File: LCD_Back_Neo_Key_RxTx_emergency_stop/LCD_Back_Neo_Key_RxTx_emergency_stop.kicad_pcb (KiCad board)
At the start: 2 copper layers, 105.5 x 101.5 mm, 23 parts, among them J1 Screw_Terminal_01x14, J2 Conn_01x20_Female, J3 Conn_01x08_Male_KeyPad, J4 Display_support_pin, J5 Display_support_pin, K1 FINDER-34.51, K2 FINDER-34.51, K3 FINDER-34.51, K4 FINDER-34.51, Q1 BC337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

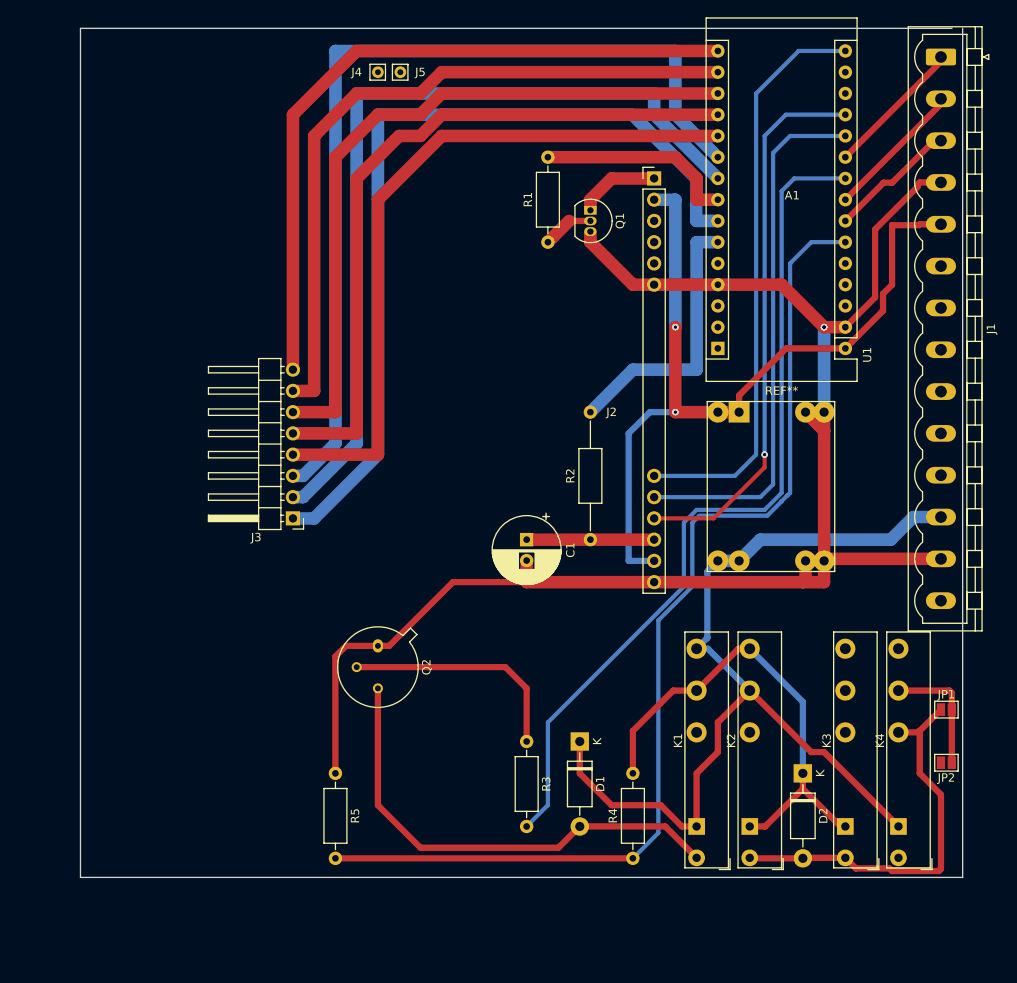
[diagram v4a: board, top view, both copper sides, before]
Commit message: contact all on PCB
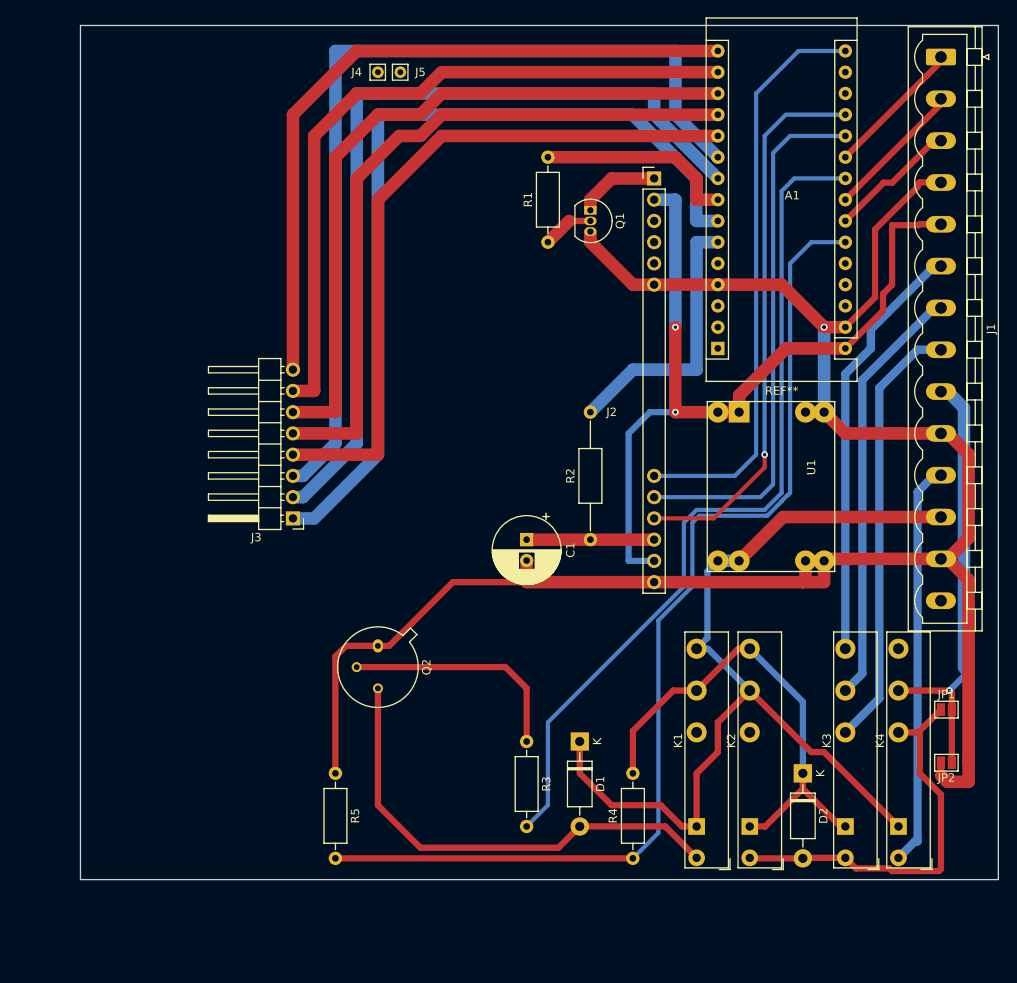
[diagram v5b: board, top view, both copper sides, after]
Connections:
- J1 pad 6: ScrewTerm8-EmrgencyRelay12 -> ScrewTerm9-EmrgencyRelay14
- J1 pad 7: ScrewTerm9-EmrgencyRelay14 -> ScrewTerm10-EmrgencyRelay11
- J1 pad 8: ScrewTerm10-EmrgencyRelay11 -> ScrewTerm8-EmrgencyRelay12
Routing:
- net ScrewTerm8-EmrgencyRelay12: track 0.00 -> 52.1 mm
- net ScrewTerm9-EmrgencyRelay14: track 0.00 -> 50.9 mm
- net ScrewTerm10-EmrgencyRelay11: track 0.00 -> 50.9 mm
- net ScrewTerm13-EmergencyStopSwitch3: track 0.00 -> 48.5 mm
- net GND: track 190.8 -> 238.3 mm
- net ScrewTerm11-EmergencyStopSwitch1: track 14.8 -> 52.9 mm, vias 0 -> 1
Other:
- board size 105.5 x 101.5 mm -> 109.7 x 102.1 mm
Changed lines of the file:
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@@
     (thickness 1.6)
     (drawings 4)
-    (tracks 238)
+    (tracks 271)
     (zones 0)
     (modules 23)
@@
   )
   (setup
-    (last_trace_width 0.75)
+    (last_trace_width 1)
     (user_trace_width 0.5)
     (user_trace_width 0.75)
+    (user_trace_width 1)
     (user_trace_width 1.5)
     (trace_clearance 0.2)
@@
     (descr "Longri ")
     (tags "Longri DCDC-Converter")
-    (fp_text reference U1 (at -4.31 -5.17 90) (layer F.SilkS)
+    (fp_text reference U1 (at 9.144 1.524 90) (layer F.SilkS)
       (effects (font (size 1 1) (thickness 0.15)))
     )
@@
       (net 10 VCC-5V))
     (pad 6 thru_hole oval (at 25 0 270) (size 2 3.6) (drill 1.4) (layers *.Cu *.Mask)
+      (net 46 ScrewTerm9-EmrgencyRelay14))
+    (pad 7 thru_hole oval (at 30 0 270) (size 2 3.6) (drill 1.4) (layers *.Cu *.Mask)
+      (net 47 ScrewTerm10-EmrgencyRelay11))
+    (pad 8 thru_hole oval (at 35 0 270) (size 2 3.6) (drill 1.4) (layers *.Cu *.Mask)
       (net 45 ScrewTerm8-EmrgencyRelay12))
-    (pad 7 thru_hole oval (at 30 0 270) (size 2 3.6) (drill 1.4) (layers *.Cu *.Mask)
-      (net 46 ScrewTerm9-EmrgencyRelay14))
-    (pad 8 thru_hole oval (at 35 0 270) (size 2 3.6) (drill 1.4) (layers *.Cu *.Mask)
-      (net 47 ScrewTerm10-EmrgencyRelay11))
     (pad 9 thru_hole oval (at 40 0 270) (size 2 3.6) (drill 1.4) (layers *.Cu *.Mask)
       (net 48 ScrewTerm11-EmergencyStopSwitch1))
@@
     )
   )
-  (gr_line (start 104.14 32.86) (end 104.14 134.36) (layer Edge.Cuts) (width 0.05))
-  (gr_line (start 208.34 32.86) (end 104.14 32.86) (layer Edge.Cuts) (width 0.05))
-  (gr_line (start 209.61 32.86) (end 209.61 134.36) (layer Edge.Cuts) (width 0.05))
-  (gr_line (start 104.14 134.36) (end 209.61 134.36) (layer Edge.Cuts) (width 0.05))
+  (gr_line (start 104.14 32.512) (end 104.14 134.62) (layer Edge.Cuts) (width 0.05))
+  (gr_line (start 213.868 32.512) (end 104.14 32.512) (layer Edge.Cuts) (width 0.05))
+  (gr_line (start 213.868 32.512) (end 213.868 134.62) (layer Edge.Cuts) (width 0.05))
+  (gr_line (start 104.14 134.62) (end 213.868 134.62) (layer Edge.Cuts) (width 0.05))
   (segment (start 185.42 63.5) (end 185.42 63.5) (width 0.25) (layer F.Cu) (net 9))
   (segment (start 157.48 96.48) (end 157.48 99.06) (width 1.5) (layer F.Cu) (net 9))
@@
   (segment (start 193.04 99.06) (end 193.04 96.52) (width 1.5) (layer F.Cu) (net 9))
   (segment (start 193.04 96.52) (end 190.82 96.52) (width 1.5) (layer F.Cu) (net 9))
-  (segment (start 193.04 80.96) (end 193.04 78.74) (width 1.5) (layer F.Cu) (net 9))
-  (segment (start 193.04 80.96) (end 190.82 78.74) (width 1.5) (layer F.Cu) (net 9))
-  (segment (start 193.04 93.98) (end 193.04 94.3) (width 1.5) (layer F.Cu) (net 9))
-  (segment (start 193.04 96.52) (end 193.04 93.98) (width 1.5) (layer F.Cu) (net 9))
-  (segment (start 193.04 93.98) (end 193.04 80.96) (width 1.5) (layer F.Cu) (net 9))
   (segment (start 190.82 96.52) (end 190.82 98.74) (width 1.5) (layer F.Cu) (net 9))
   (segment (start 190.82 98.74) (end 190.5 99.06) (width 1.5) (layer F.Cu) (net 9))
@@
   (segment (start 199.136 65.024) (end 199.136 56.896) (width 0.75) (layer F.Cu) (net 9))
   (segment (start 195.58 68.58) (end 199.136 65.024) (width 0.75) (layer F.Cu) (net 9))
+  (segment (start 207.81 81.28) (end 207.01 81.28) (width 1.5) (layer F.Cu) (net 9))
+  (segment (start 210.31 83.78) (end 207.81 81.28) (width 1.5) (layer F.Cu) (net 9))
+  (segment (start 210.31 93.78) (end 210.31 83.78) (width 1.5) (layer F.Cu) (net 9))
+  (segment (start 207.81 96.28) (end 210.31 93.78) (width 1.5) (layer F.Cu) (net 9))
+  (segment (start 207.01 96.28) (end 207.81 96.28) (width 1.5) (layer F.Cu) (net 9))
+  (segment (start 207.81 96.28) (end 210.312 98.782) (width 1.5) (layer F.Cu) (net 9))
+  (segment (start 210.312 98.782) (end 210.312 120.396) (width 1.5) (layer F.Cu) (net 9))
+  (segment (start 210.312 120.396) (end 210.312 122.936) (width 1.5) (layer F.Cu) (net 9))
+  (segment (start 210.312 122.936) (end 210.312 122.936) (width 1.5) (layer F.Cu) (net 9))
+  (segment (start 210.312 122.936) (end 207.772 122.936) (width 1.5) (layer F.Cu) (net 9))
+  (segment (start 207.01 122.174) (end 207.01 120.65) (width 0.75) (layer F.Cu) (net 9))
+  (segment (start 207.772 122.936) (end 207.01 122.174) (width 1.5) (layer F.Cu) (net 9))
+  (segment (start 195.58 81.28) (end 193.04 78.74) (width 1.5) (layer F.Cu) (net 9))
+  (segment (start 207.01 81.28) (end 195.58 81.28) (width 1.5) (layer F.Cu) (net 9))
+  (segment (start 190.82 78.74) (end 193.04 78.74) (width 1.5) (layer F.Cu) (net 9))
   (segment (start 180.34 78.74) (end 182.88 78.74) (width 1.5) (layer F.Cu) (net 10))
   (segment (start 180.34 78.74) (end 175.26 78.74) (width 1.5) (layer F.Cu) (net 10))
@@
   (segment (start 201.168 63.5) (end 200.08601 64.58199) (width 0.75) (layer F.Cu) (net 10))
   (segment (start 201.168 56.388) (end 201.168 63.5) (width 0.75) (layer F.Cu) (net 10))
-  (segment (start 182.88 76.74) (end 188.5 71.12) (width 0.75) (layer F.Cu) (net 10))
-  (segment (start 182.88 78.74) (end 182.88 76.74) (width 0.75) (layer F.Cu) (net 10))
-  (segment (start 188.5 71.12) (end 195.58 71.12) (width 0.75) (layer F.Cu) (net 10))
+  (segment (start 182.88 76.74) (end 188.5 71.12) (width 1.5) (layer F.Cu) (net 10))
+  (segment (start 182.88 78.74) (end 182.88 76.74) (width 1.5) (layer F.Cu) (net 10))
+  (segment (start 188.5 71.12) (end 195.58 71.12) (width 1.5) (layer F.Cu) (net 10))
   (segment (start 180.34 58.42) (end 177.8 58.42) (width 1.5) (layer B.Cu) (net 11))
   (segment (start 177.8 58.42) (end 177.8 73.66) (width 1.5) (layer B.Cu) (net 11))
@@
   (segment (start 193.04 119.38) (end 200.66 127) (width 0.75) (layer F.Cu) (net 34))
   (segment (start 200.66 127) (end 201.93 128.27) (width 0.75) (layer F.Cu) (net 34))
-  (segment (start 203.71 91.28) (end 201.01 93.98) (width 1.5) (layer B.Cu) (net 34))
-  (segment (start 207.01 91.28) (end 203.71 91.28) (width 1.5) (layer B.Cu) (net 34))
-  (segment (start 185.42 93.98) (end 182.88 96.52) (width 1.5) (layer B.Cu) (net 34))
-  (segment (start 201.01 93.98) (end 185.42 93.98) (width 1.5) (layer B.Cu) (net 34))
   (segment (start 178.999999 105.820001) (end 177.8 107.02) (width 0.75) (layer B.Cu) (net 34))
   (segment (start 179.090001 105.729999) (end 178.999999 105.820001) (width 0.75) (layer B.Cu) (net 34))
   (segment (start 179.090001 97.769999) (end 179.090001 105.729999) (width 0.75) (layer B.Cu) (net 34))
   (segment (start 180.34 96.52) (end 179.090001 97.769999) (width 0.75) (layer B.Cu) (net 34))
+  (segment (start 188.12 91.28) (end 182.88 96.52) (width 1.5) (layer F.Cu) (net 34))
+  (segment (start 207.01 91.28) (end 188.12 91.28) (width 1.5) (layer F.Cu) (net 34))
   (segment (start 157.48 111.76) (end 157.48 118.11) (width 0.75) (layer F.Cu) (net 37))
   (segment (start 137.16 109.22) (end 154.94 109.22) (width 0.75) (layer F.Cu) (net 37))
@@
   (segment (start 207.01 133.35) (end 207.01 124.46) (width 0.75) (layer F.Cu) (net 44))
   (segment (start 204.47 116.84) (end 207.01 114.3) (width 0.75) (layer F.Cu) (net 44))
+  (segment (start 199.644 112.956) (end 195.58 117.02) (width 1) (layer B.Cu) (net 45))
+  (segment (start 199.644 75.846) (end 199.644 112.956) (width 1) (layer B.Cu) (net 45))
+  (segment (start 207.01 71.28) (end 204.21 71.28) (width 1) (layer B.Cu) (net 45))
+  (segment (start 204.21 71.28) (end 199.644 75.846) (width 1) (layer B.Cu) (net 45))
+  (segment (start 206.21 61.28) (end 198.628 68.862) (width 1) (layer B.Cu) (net 46))
+  (segment (start 207.01 61.28) (end 206.21 61.28) (width 1) (layer B.Cu) (net 46))
+  (segment (start 198.628 68.862) (end 198.628 71.12) (width 1) (layer B.Cu) (net 46))
+  (segment (start 198.628 71.12) (end 195.58 74.168) (width 1) (layer B.Cu) (net 46))
+  (segment (start 195.58 74.168) (end 195.58 107.02) (width 1) (layer B.Cu) (net 46))
+  (segment (start 197.612 109.988) (end 195.58 112.02) (width 1) (layer B.Cu) (net 47))
+  (segment (start 197.612 74.878) (end 197.612 109.988) (width 1) (layer B.Cu) (net 47))
+  (segment (start 207.01 66.28) (end 206.21 66.28) (width 1) (layer B.Cu) (net 47))
+  (segment (start 206.21 66.28) (end 197.612 74.878) (width 1) (layer B.Cu) (net 47))
   (segment (start 201.93 112.02) (end 208.02 112.02) (width 0.75) (layer F.Cu) (net 48))
   (segment (start 208.31 112.31) (end 208.31 114.3) (width 0.75) (layer F.Cu) (net 48))
   (segment (start 208.02 112.02) (end 208.31 112.31) (width 0.75) (layer F.Cu) (net 48))
   (segment (start 208.31 114.3) (end 208.31 120.65) (width 0.75) (layer F.Cu) (net 48))
+  (segment (start 209.76001 78.23001) (end 209.76001 109.26399) (width 1.5) (layer B.Cu) (net 48))
+  (segment (start 207.01 76.28) (end 207.81 76.28) (width 1.5) (layer B.Cu) (net 48))
+  (segment (start 207.81 76.28) (end 209.76001 78.23001) (width 1.5) (layer B.Cu) (net 48))
+  (segment (start 208.02 112.02) (end 208.02 112.02) (width 0.75) (layer F.Cu) (net 48))
+  (via (at 208.02 112.02) (size 0.8) (drill 0.4) (layers F.Cu B.Cu) (net 48))
+  (segment (start 209.76001 110.27999) (end 208.02 112.02) (width 0.75) (layer B.Cu) (net 48))
+  (segment (start 209.76001 109.26399) (end 209.76001 110.27999) (width 0.75) (layer B.Cu) (net 48))
+  (segment (start 206.21 86.28) (end 204.216 88.274) (width 1) (layer B.Cu) (net 49))
+  (segment (start 207.01 86.28) (end 206.21 86.28) (width 1) (layer B.Cu) (net 49))
+  (segment (start 204.216 88.274) (end 204.216 130.048) (width 1) (layer B.Cu) (net 49))
+  (segment (start 203.902 130.048) (end 201.93 132.02) (width 1) (layer B.Cu) (net 49))
+  (segment (start 204.216 130.048) (end 203.902 130.048) (width 1) (layer B.Cu) (net 49))
 )

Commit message: move keyboard connector
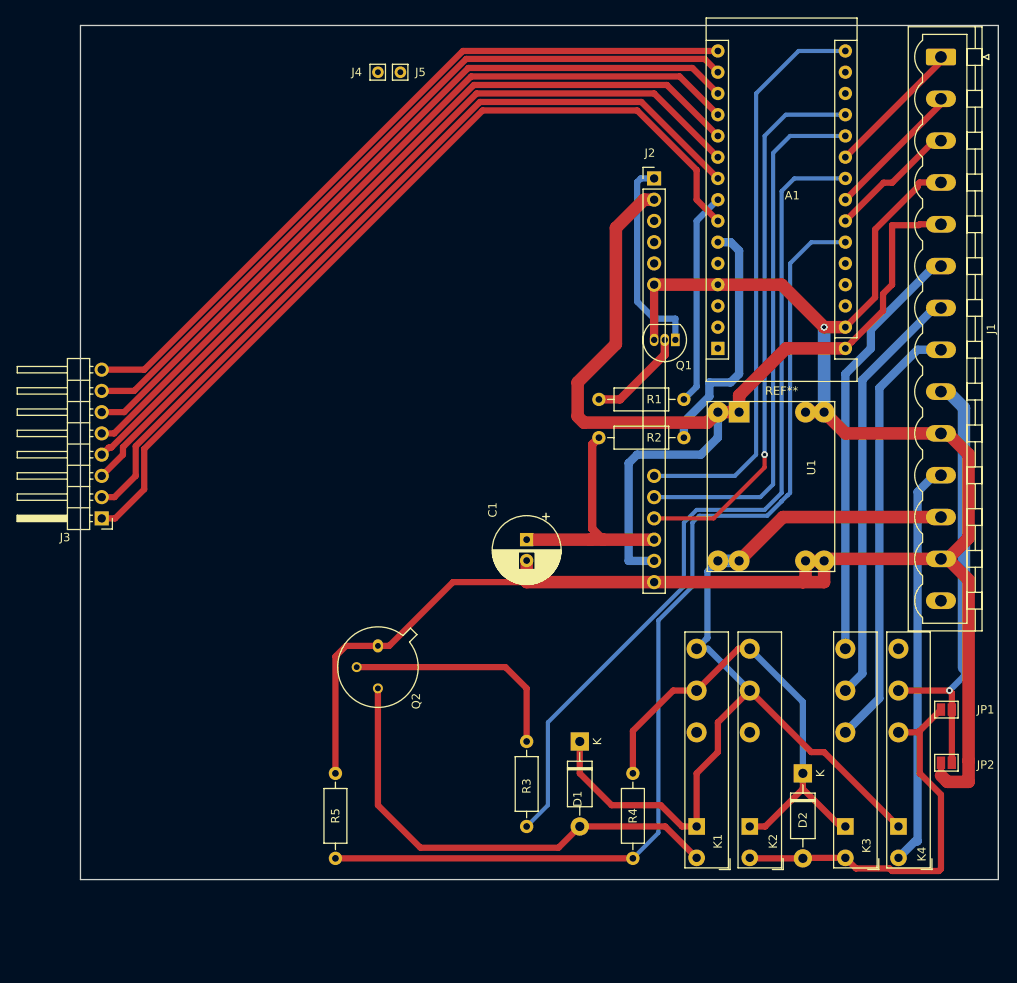
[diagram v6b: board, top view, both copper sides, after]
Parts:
- R2: footprint Resistor_THT:R_Axial_DIN0207_L6.3mm_D2.5mm_P15.24mm_Horizontal -> Resistor_THT:R_Axial_DIN0207_L6.3mm_D2.5mm_P10.16mm_Horizontal
- moved J3 22.9 mm to (106.7, 91.4)
- moved R1 19.8 mm to (166.1, 77.2), turned to 0 degrees
- moved Q1 18.5 mm to (175.3, 70.1), turned to 180 degrees
- moved R2 12.2 mm to (166.1, 81.8), turned to 0 degrees
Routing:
- net VCC-5V: track 100.4 -> 120.2 mm, vias 2 -> 0
- net Net-(J2-Pad1): track 9.74 -> 24.5 mm
- net Net-(C1-Pad1): track 15.2 -> 28.3 mm
- net Ardu_D7: track 109.1 -> 96.3 mm
- net Ardu_D8: track 84.4 -> 94.5 mm
- net Ardu_D9: track 84.4 -> 93.2 mm
- net Ardu_D10: track 84.4 -> 92.0 mm
- net Ardu_D11: track 84.4 -> 90.8 mm
- net Net-(Q1-Pad2): track 6.13 -> 11.8 mm
- net Ardu_D12: track 84.4 -> 89.4 mm
- net GND: track 238.3 -> 234.2 mm
- net Ardu_D3: track 32.6 -> 29.5 mm
- net Ardu_D6: track 101.0 -> 99.1 mm
- net Ardu_D5: track 23.9 -> 25.6 mm
- net Ardu_D4: track 102.8 -> 104.2 mm

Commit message: add mouting holes
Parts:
- added  : , Socket_Arduino_Micro:1pin_Micro, F.Cu at (173.8, 126.5)
- added  : , Socket_Arduino_Micro:1pin_Micro, F.Cu at (108.4, 37.6)
- added  : , Socket_Arduino_Micro:1pin_Micro, F.Cu at (173.8, 38.1)
- added  : , Socket_Arduino_Micro:1pin_Micro, F.Cu at (108.4, 126.0)
- moved D1 14.2 mm to (152.1, 110.0)
- moved R4 14.2 mm to (158.5, 124.0)
- moved Q2 14.2 mm to (128.0, 98.6)
- moved R3 14.2 mm to (145.8, 110.0)
- moved R5 14.2 mm to (122.9, 113.8)
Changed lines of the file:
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@@
     (tracks 276)
     (zones 0)
-    (modules 23)
+    (modules 27)
     (nets 52)
   )
@@
     (47 F.CrtYd user)
     (48 B.Fab user)
-    (49 F.Fab user hide)
+    (49 F.Fab user)
   )
   (setup
-    (last_trace_width 1)
+    (last_trace_width 0.25)
     (user_trace_width 0.5)
     (user_trace_width 0.75)
@@
     (mod_text_size 1 1)
     (mod_text_width 0.15)
-    (pad_size 1 1)
-    (pad_drill 1)
+    (pad_size 4 4)
+    (pad_drill 3.1)
     (pad_to_mask_clearance 0.051)
     (solder_mask_min_width 0.25)
-    (aux_axis_origin 0 0)
+    (aux_axis_origin 104.14 134.61746)
     (visible_elements 7FFFFFFF)
     (pcbplotparams
@@
     (add_net VCC-24V)
     (add_net VCC-5V)
+  )
+  (module Socket_Arduino_Micro:1pin_Micro (layer F.Cu)
+    (at 173.75886 126.54026)
+    (descr "module 1 pin (ou trou mecanique de percage)")
+    (tags DEV)
+    (fp_text reference " " (at 0 0) (layer F.SilkS) hide
+      (effects (font (size 1 1) (thickness 0.15)))
+    )
+    (fp_text value " " (at 0 1.397) (layer F.Fab)
+      (effects (font (size 1 1) (thickness 0.15)))
+    )
+    (pad 1 thru_hole circle (at 0 0) (size 4 4) (drill 3.1) (layers *.Cu *.Mask F.SilkS))
+  )
+  (module Socket_Arduino_Micro:1pin_Micro (layer F.Cu)
+    (at 108.37926 37.6428)
+    (descr "module 1 pin (ou trou mecanique de percage)")
+    (tags DEV)
+    (fp_text reference " " (at 0 0) (layer F.SilkS) hide
+      (effects (font (size 1 1) (thickness 0.15)))
+    )
+    (fp_text value " " (at 0 1.397) (layer F.Fab)
+      (effects (font (size 1 1) (thickness 0.15)))
+    )
+    (pad 1 thru_hole circle (at 0 0) (size 4 4) (drill 3.1) (layers *.Cu *.Mask F.SilkS))
+  )
+  (module Socket_Arduino_Micro:1pin_Micro (layer F.Cu)
+    (at 173.75886 38.14826)
+    (descr "module 1 pin (ou trou mecanique de percage)")
+    (tags DEV)
+    (fp_text reference " " (at 0 0) (layer F.SilkS) hide
+      (effects (font (size 1 1) (thickness 0.15)))
+    )
+    (fp_text value " " (at 0 1.397) (layer F.Fab)
+      (effects (font (size 1 1) (thickness 0.15)))
+    )
+    (pad 1 thru_hole circle (at 0 0) (size 4 4) (drill 3.1) (layers *.Cu *.Mask F.SilkS))
+  )
+  (module Socket_Arduino_Micro:1pin_Micro (layer F.Cu)
+    (at 108.37926 126.0348)
+    (descr "module 1 pin (ou trou mecanique de percage)")
+    (tags DEV)
+    (fp_text reference " " (at 0 0) (layer F.SilkS) hide
+      (effects (font (size 1 1) (thickness 0.15)))
+    )
+    (fp_text value " " (at 0 1.397) (layer F.Fab)
+      (effects (font (size 1 1) (thickness 0.15)))
+    )
+    (pad 1 thru_hole circle (at 0 0) (size 4 4) (drill 3.1) (layers *.Cu *.Mask F.SilkS))
   )
   (module Module:Arduino_Nano_Miror (layer F.Cu)
@@
   )
   (module Package_TO_SOT_THT:TO-39-3 (layer F.Cu)
-    (at 139.7 106.68 270)
+    (at 128.016 98.552 270)
     (descr TO-39-3)
     (tags TO-39-3)
@@
   )
   (module Resistor_THT:R_Axial_DIN0207_L6.3mm_D2.5mm_P10.16mm_Horizontal (layer F.Cu)
-    (at 157.48 118.11 270)
+    (at 145.796 109.982 270)
     (descr "Resistor, Axial_DIN0207 series, Axial, Horizontal, pin pitch=10.16mm, 0.25W = 1/4W, length*diameter=6.3*2.5mm^2, http://cdn-reichelt.de/documents/datenblatt/B400/1_4W%23YAG.pdf")
     (tags "Resistor Axial_DIN0207 series Axial Horizontal pin pitch 10.16mm 0.25W = 1/4W length 6.3mm diameter 2.5mm")
@@
   )
   (module Resistor_THT:R_Axial_DIN0207_L6.3mm_D2.5mm_P10.16mm_Horizontal (layer F.Cu)
-    (at 170.18 132.08 90)
+    (at 158.496 123.952 90)
     (descr "Resistor, Axial_DIN0207 series, Axial, Horizontal, pin pitch=10.16mm, 0.25W = 1/4W, length*diameter=6.3*2.5mm^2, http://cdn-reichelt.de/documents/datenblatt/B400/1_4W%23YAG.pdf")
     (tags "Resistor Axial_DIN0207 series Axial Horizontal pin pitch 10.16mm 0.25W = 1/4W length 6.3mm diameter 2.5mm")
@@
   )
   (module Resistor_THT:R_Axial_DIN0207_L6.3mm_D2.5mm_P10.16mm_Horizontal (layer F.Cu)
-    (at 134.62 121.92 270)
+    (at 122.936 113.792 270)
     (descr "Resistor, Axial_DIN0207 series, Axial, Horizontal, pin pitch=10.16mm, 0.25W = 1/4W, length*diameter=6.3*2.5mm^2, http://cdn-reichelt.de/documents/datenblatt/B400/1_4W%23YAG.pdf")
     (tags "Resistor Axial_DIN0207 series Axial Horizontal pin pitch 10.16mm 0.25W = 1/4W length 6.3mm diameter 2.5mm")
@@
   )
   (module Diode_THT:D_DO-41_SOD81_P10.16mm_Horizontal (layer F.Cu)
-    (at 163.83 118.11 270)
+    (at 152.146 109.982 270)
     (descr "Diode, DO-41_SOD81 series, Axial, Horizontal, pin pitch=10.16mm, , length*diameter=5.2*2.7mm^2, , http://www.diodes.com/_files/packages/DO-41%20(Plastic).pdf")
     (tags "Diode DO-41_SOD81 series Axial Horizontal pin pitch 10.16mm  length 5.2mm diameter 2.7mm")
